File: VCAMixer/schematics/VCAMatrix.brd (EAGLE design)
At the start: 120 x 100 mm, 293 parts, among them IC1 QUAD_OPAMPD, IC2 TL074D, IC4 TL072D, Q1 BC846ALT1SMD, Q10 BSS123, Q2 BC846ALT1SMD, Q3 BC846ALT1SMD, Q4 BC846ALT1SMD, Q5 BC846ALT1SMD, Q6 BC846ALT1SMD, Q7 BC846ALT1SMD, Q8 BC846ALT1SMD, Q9 BSS84, X1 53048-05, X2 53048-05

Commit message: Board and Schematic Updated
Begin routing for input and output circuitry.
Schottky Diode used for power rail protection.
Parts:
- removed VCA1:D1, VCA2:D1, VCA3:D1, VCA4:D1: B130LAW-7-F, diode:SOD123
- added D3: BAT54A, diode:SOT23
- U$1, U$2: value RTRIM-3362P -> (none); device GeekAmmo:RTRIM3362P -> resistor:RTRIM64W
- moved R42 275.3 mm to (117.2, 17.8), turned to 90 degrees
- moved JP1 260.4 mm to (99.1, 76.2)
- moved R38 260.0 mm to (91.4, -16.5)
- moved VCA4:R3 246.1 mm to (117.2, 21.6), turned to 90 degrees
- moved VCA1:R3 243.4 mm to (114.3, 80.0), turned to 90 degrees
- moved JP3 242.9 mm to (72.4, 76.2)
- moved Q2 242.3 mm to (150.4, -30.9)
- moved VCA3:R3 239.2 mm to (117.6, 40.9), turned to 90 degrees
- moved VCA2:R3 238.8 mm to (117.2, 61.0), turned to 90 degrees
- moved VCA4:C14 238.4 mm to (117.2, 25.7), turned to 90 degrees
- moved VCA2:C14 238.3 mm to (118.1, 65.1), turned to 90 degrees
- moved C3 238.3 mm to (78.7, -16.5)
- moved C4 238.3 mm to (73.7, -16.5)
- moved C5 238.3 mm to (68.6, -16.5)
- moved C6 238.3 mm to (63.5, -16.5)
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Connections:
- net -12V: now also D3.3; no longer VCA1:D1.A, VCA2:D1.A, VCA3:D1.A, VCA4:D1.A
- net GND: now also D3.1, D3.2; no longer VCA1:D1.C, VCA2:D1.C, VCA3:D1.C, VCA4:D1.C
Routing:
- net -12V: track 0.00 -> 223.6 mm, vias 0 -> 7
- net +12V: track 0.00 -> 221.1 mm, vias 0 -> 13
- net CV_DD: track 0.00 -> 104.4 mm, vias 0 -> 1
- net GND: track 0.00 -> 78.7 mm, vias 0 -> 49
- net N$34: track 0.00 -> 76.2 mm, vias 0 -> 3
- net VCA4:IC2_4: track 0.00 -> 66.8 mm, vias 0 -> 2
- net VCA3:IC2_4: track 0.00 -> 66.5 mm, vias 0 -> 2
- net VCA2:IC2_5: track 0.00 -> 57.2 mm
- net CV_DB: track 0.00 -> 54.7 mm, vias 0 -> 1
- net CV_DC: track 0.00 -> 52.8 mm, vias 0 -> 1
- net CV_DA: track 0.00 -> 51.8 mm, vias 0 -> 1
- net N$18: track 0.00 -> 51.2 mm, vias 0 -> 4
- net N$82: track 0.00 -> 46.2 mm, vias 0 -> 3
- net VCA3:IC2_2: track 0.00 -> 41.8 mm
- net VCA1:IC2_2: track 0.00 -> 41.8 mm, vias 0 -> 2
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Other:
- board size 120 x 100 mm -> 119.8 x 101.3 mm

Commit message: Latest update on VCA Matrix Board
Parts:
- moved Q9 191.0 mm to (111.0, 22.5)
- moved R5 107.1 mm to (109.9, 96.8)
- moved R3 105.7 mm to (77.5, 80.0), turned to 270 degrees
- moved R13 102.5 mm to (81.3, 51.4), turned to 180 degrees
- moved R14 93.5 mm to (78.7, 37.8), turned to 270 degrees
- moved R6 92.5 mm to (102.6, 81.3), turned to 270 degrees
- moved R2 90.3 mm to (77.5, 57.8), turned to 270 degrees
- moved R10 85.9 mm to (107.7, 53.5), turned to 270 degrees
- moved Q2 82.7 mm to (75.8, 4.70), turned to 180 degrees
- moved R19 80.8 mm to (75.9, 38.4), turned to 180 degrees
- moved R15 67.4 mm to (109.6, 38.2), turned to 180 degrees
- moved R16 67.1 mm to (106.4, 38.4), turned to 180 degrees
- moved Q3 65.2 mm to (79.4, 4.76), turned to 180 degrees
- moved R1 64.5 mm to (80.0, 7.94), turned to 180 degrees
- moved R40 63.5 mm to (72.7, 49.2), turned to 180 degrees
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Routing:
- net N$34: track 76.2 -> 226.4 mm, vias 3 -> 17
- net -12V: track 223.6 -> 358.3 mm, vias 7 -> 13
- net N$47: track 0.00 -> 107.7 mm, vias 0 -> 6
- net N$11: track 0.00 -> 106.9 mm, vias 0 -> 11
- net CV_DD: track 104.4 -> 4.23 mm, vias 1 -> 0
- net N$82: track 46.2 -> 132.5 mm, vias 3 -> 4
- net N$58: track 2.32 -> 86.7 mm, vias 0 -> 6
- net CLAMP_REF: track 30.8 -> 110.3 mm, vias 0 -> 4
- net N$3: track 28.9 -> 104.1 mm, vias 3 -> 6
- net +12V: track 221.1 -> 290.9 mm, vias 13 -> 24
- net N$8: track 5.45 -> 67.6 mm, vias 0 -> 2
- net N$33: track 0.00 -> 60.4 mm, vias 0 -> 1
- net N$78: track 0.00 -> 52.6 mm, vias 0 -> 2
- net N$24: track 0.00 -> 52.2 mm, vias 0 -> 2
- net N$54: track 0.00 -> 43.2 mm, vias 0 -> 2
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
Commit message: Latest Update To VCA Board
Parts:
- moved R45 31.8 mm to (73.8, 1.65)
- moved R47 26.7 mm to (86.2, 11.2)
- moved Q7 18.9 mm to (99.9, 2.60)
- moved VCA1:R13 18.7 mm to (76.0, 79.1)
- moved VCA4:R43 16.1 mm to (84.3, 78.5)
- moved R35 14.4 mm to (67.8, 15.6)
- moved VCA4:R15 12.7 mm to (71.9, 20.1), turned to 90 degrees
- moved VCA2:C1 12.3 mm to (90.0, 73.4), turned to 180 degrees
- moved R17 12.2 mm to (97.0, 15.6)
- moved C2 12.2 mm to (98.6, 8.63)
- moved R41 12.2 mm to (100.5, 8.63)
- moved VCA1:R21 11.9 mm to (77.4, 81.8)
- moved VCA1:R9 11.9 mm to (74.2, 81.8)
- moved VCA3:R13 11.7 mm to (60.8, 74.3)
- moved VCA1:R15 11.6 mm to (72.0, 81.8)
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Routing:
- net GND: track 83.5 -> 225.9 mm, vias 52 -> 62
- net +12V: track 290.9 -> 317.8 mm, vias 24 -> 28
- net N$3: track 104.1 -> 130.2 mm, vias 6 -> 8
- net N$60: track 3.21 -> 21.7 mm, vias 0 -> 2
- net N$11: track 106.9 -> 90.4 mm, vias 11 -> 10
- net VCA4:N$7: track 7.20 -> 22.0 mm
- net CV_AA: track 3.99 -> 13.0 mm
- net VCA4:IC2_4: track 62.2 -> 71.1 mm
- net N$51: track 0.00 -> 7.67 mm
- net CV_DC: track 13.1 -> 6.67 mm
- net VCA1:IC2_5: track 19.7 -> 13.6 mm
- net N$24: track 52.2 -> 57.6 mm
- net OUTPUT_B: track 21.0 -> 26.3 mm, vias 1 -> 2
- net N$22: track 33.7 -> 28.4 mm
- net IN_A: track 0.00 -> 4.98 mm
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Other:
- board size 119.8 x 101.3 mm -> 116 x 100.3 mm

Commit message: Bottom Board Completed
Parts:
- moved R45 28.4 mm to (96.7, 18.5)
- moved R47 18.5 mm to (104.6, 9.59), turned to 270 degrees
- moved R33 17.9 mm to (97.1, 15.5), turned to 180 degrees
- moved R37 16.4 mm to (106.2, 13.1), turned to 270 degrees
- moved R7 11.6 mm to (83.5, 10.9)
- moved C5 8.91 mm to (87.5, 1.97)
- moved C2 8.90 mm to (103.7, 1.33), turned to 0 degrees
- moved R17 7.25 mm to (99.9, 8.95), turned to 270 degrees
- moved R24 6.38 mm to (76.4, 10.5)
- moved C3 6.30 mm to (67.8, 20.1), turned to 270 degrees
- moved R41 5.93 mm to (94.8, 10.2), turned to 180 degrees
- moved R23 5.84 mm to (91.6, 10.2), turned to 180 degrees
- moved C4 5.13 mm to (87.5, 3.24)
- moved C1 4.77 mm to (65.3, 1.97), turned to 180 degrees
- moved R12 2.54 mm to (70.3, 9.59)
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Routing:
- net GND: track 225.9 -> 321.7 mm, vias 62 -> 76
- net +12V: track 317.8 -> 387.0 mm, vias 28 -> 32
- net OUTPUT_B: track 26.3 -> 80.7 mm, vias 2 -> 4
- net N$66: track 0.38 -> 49.2 mm, vias 0 -> 4
- net N$59: track 30.1 -> 74.3 mm, vias 1 -> 3
- net -12V: track 355.3 -> 399.1 mm, vias 13 -> 19
- net OUTPUT_A: track 0.00 -> 41.2 mm, vias 0 -> 2
- net N$58: track 87.6 -> 127.1 mm, vias 6 -> 8
- net N$11: track 90.4 -> 118.1 mm, vias 10 -> 11
- net N$22: track 28.4 -> 54.8 mm, vias 3 -> 6
- net OUTPUT_C: track 0.00 -> 25.6 mm, vias 0 -> 2
- net N$47: track 108.2 -> 131.6 mm, vias 6 -> 7
- net N$45: track 0.00 -> 20.5 mm, vias 0 -> 2
- net IN_A: track 4.98 -> 24.6 mm, vias 0 -> 2
- net N$82: track 133.3 -> 152.1 mm
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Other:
- board size 116 x 100.3 mm -> 114.8 x 100 mm

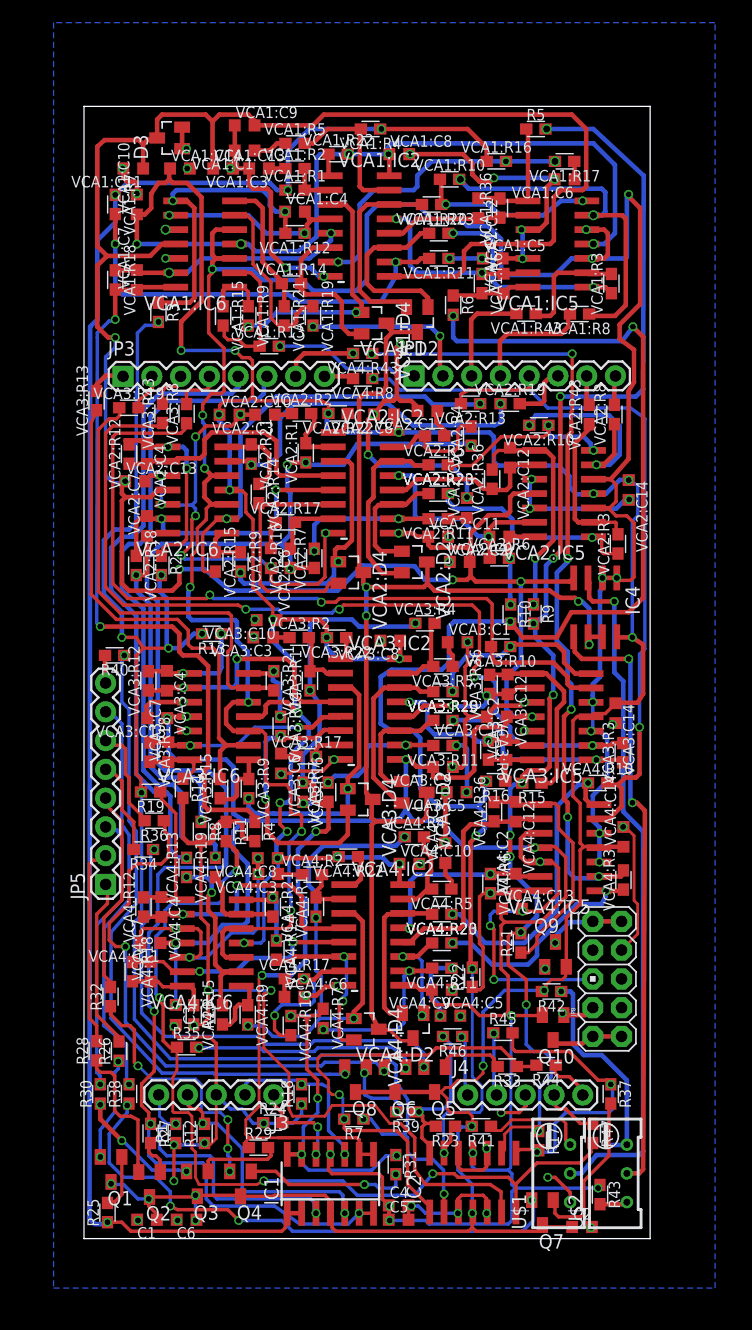
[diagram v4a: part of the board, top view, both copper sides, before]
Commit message: added top ground plane and ajusted routing
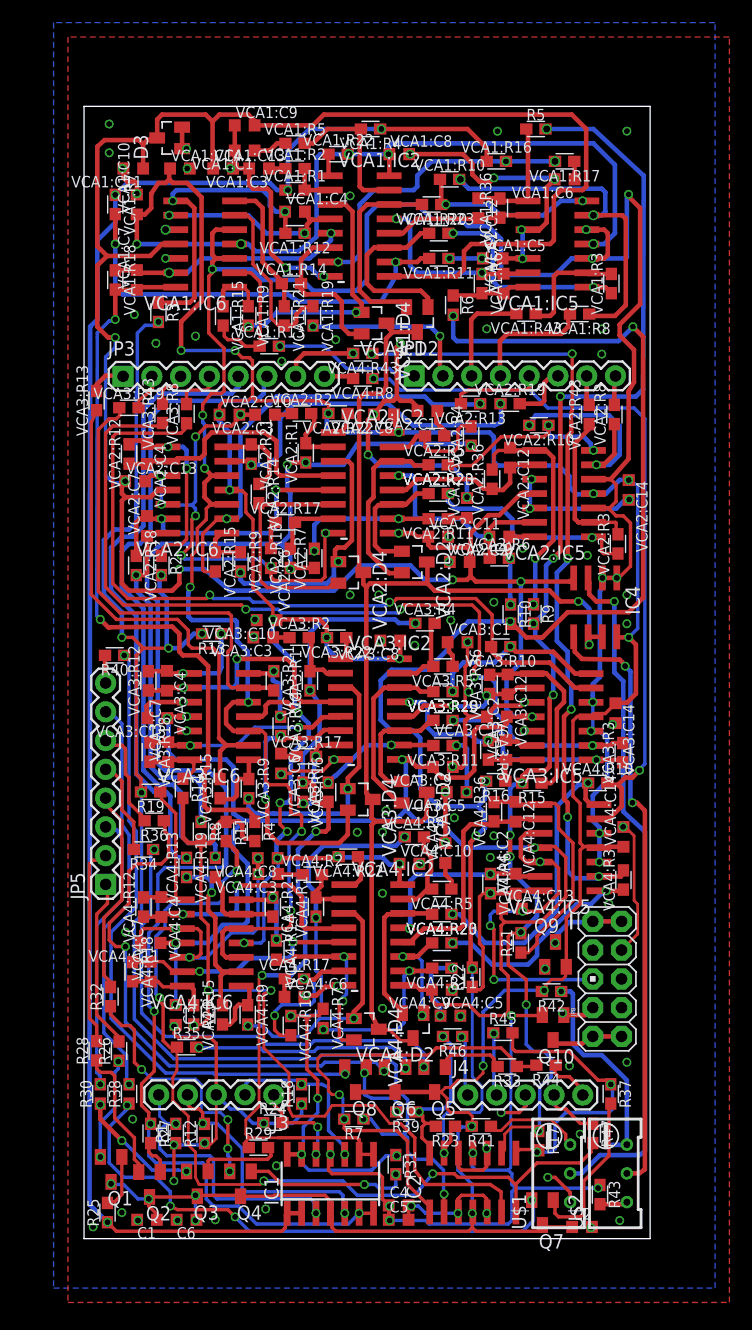
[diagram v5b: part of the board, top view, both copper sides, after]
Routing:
- net N$47: track 131.6 -> 129.5 mm
- net VCA3:IC2_2: track 71.9 -> 70.9 mm
- net -12V: track 399.1 -> 398.0 mm
- net N$34: track 230.4 -> 229.3 mm
- net VCA3:N$23: track 12.2 -> 11.4 mm
- net VCA3:IC2_1: track 16.6 -> 15.8 mm
- net OUTPUT_B: track 80.7 -> 80.1 mm
- net N$49: track 12.6 -> 12.0 mm
- net N$23: track 77.4 -> 76.8 mm
- net VCA2:N$7: track 21.8 -> 21.3 mm
- net GND: track 321.7 -> 321.2 mm, vias 76 -> 119
- net N$13: track 9.77 -> 9.22 mm
- net CLAMP_REF: track 106.5 -> 106.6 mm, vias 4 -> 2
- added copper zone on layer 1, net GND

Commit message: Routing completed for Top Board
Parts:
- moved X2 4.45 mm to (5.78, 38.9), turned to 90 degrees
- turned X1 to 270 degrees
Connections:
- removed net N$80: OUTD.P$3
- removed net N$81: OUTC.P$3
- removed net N$83: OUTB.P$3
- removed net N$84: OUTA.P$3
- net OUT_A: now also OUTA.P$3
- net OUT_B: now also OUTB.P$3
- net OUT_C: now also OUTC.P$3
- net OUT_D: now also OUTD.P$3
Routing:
- net LED_8: track 2.45 -> 66.5 mm
- net OUT_A: track 4.24 -> 67.3 mm
- net LED_3: track 24.7 -> 79.1 mm
- net N$75: track 0.00 -> 54.2 mm
- net N$76: track 0.00 -> 50.3 mm, vias 0 -> 1
- net LED_4: track 18.4 -> 68.7 mm, vias 0 -> 1
- net N$74: track 0.00 -> 48.5 mm
- net CV_DD: track 2.61 -> 47.0 mm
- net N$70: track 0.00 -> 44.2 mm, vias 0 -> 1
- net CV_AA: track 13.0 -> 57.2 mm
- net CV_BA: track 8.10 -> 51.2 mm
- net CV_CD: track 4.25 -> 46.6 mm
- net LED_7: track 35.8 -> 76.4 mm
- net N$73: track 0.00 -> 39.9 mm, vias 0 -> 1
- net OUT_B: track 5.09 -> 44.7 mm
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
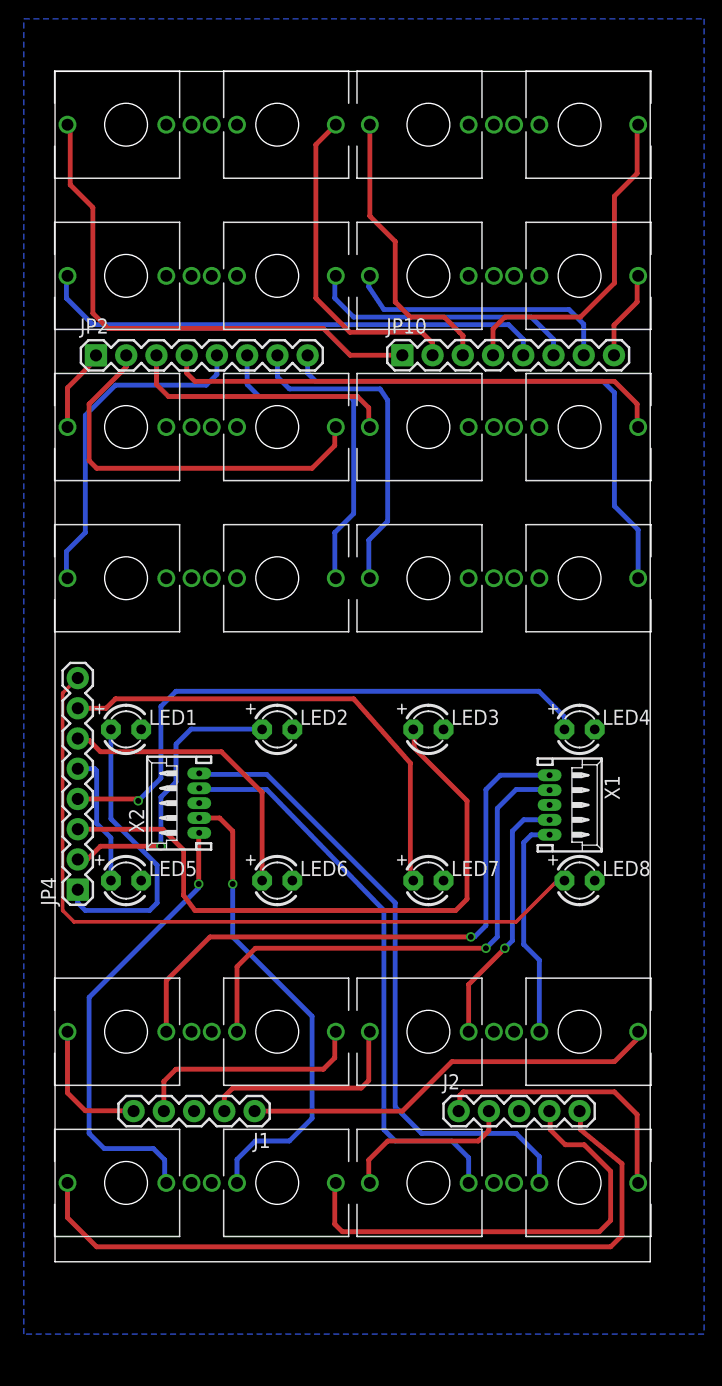
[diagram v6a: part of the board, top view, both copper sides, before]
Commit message: added in/out headers and routing
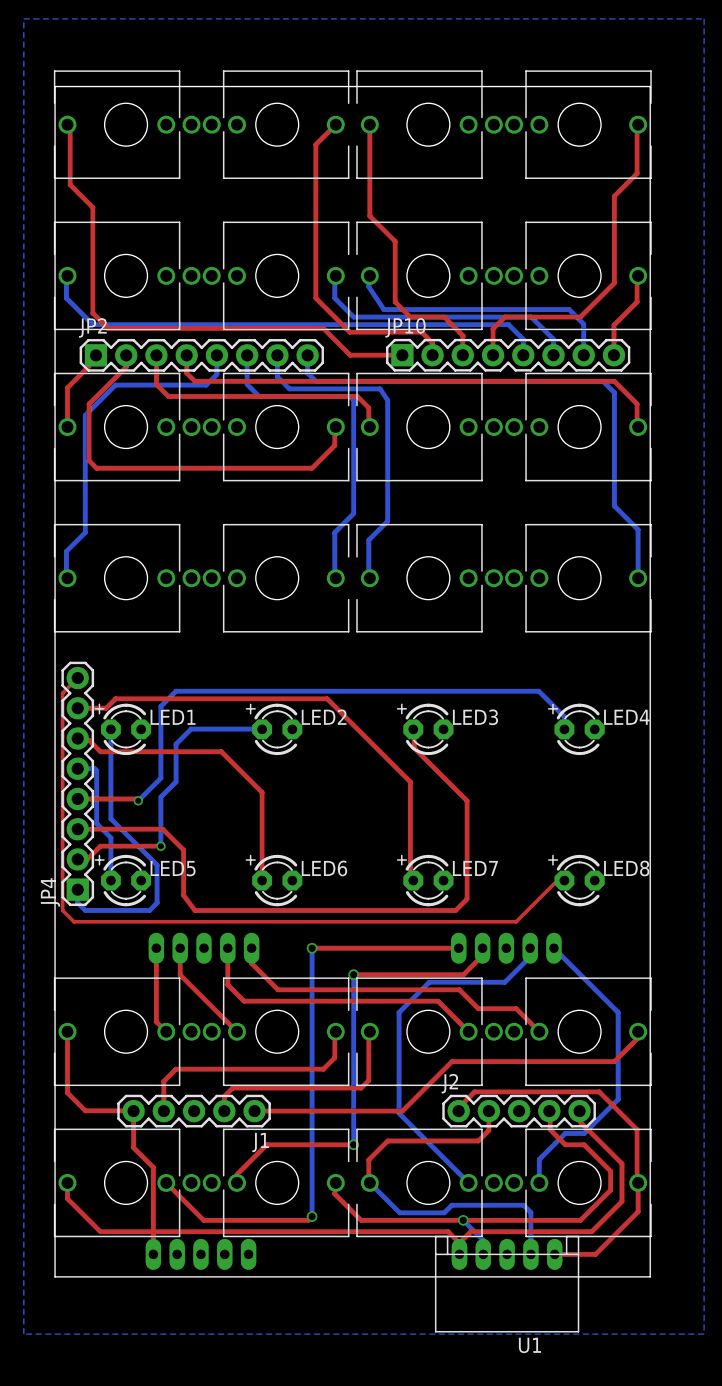
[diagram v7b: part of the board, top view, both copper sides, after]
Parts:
- removed X1, X2: 53048-05, con-molex:53048-05
- added U1, U2, U3, U4: CON-JST_PH_5W, Rebel:CON-JST_PH_5W
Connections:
- net GND: now also U1.P3, U2.P3, U3.P3, U4.P3; no longer X1.3, X2.3
- net IN_A: now also U2.P1
- net IN_B: now also U2.P2
- net IN_C: now also U2.P4
- net IN_D: now also U2.P5
- net N$55: now also U3.P5; no longer X2.5
- net N$70: now also U4.P4; no longer X1.4
- net N$71: now also U4.P2; no longer X1.2
- net N$72: now also U4.P1; no longer X1.1
- net N$73: now also U3.P4; no longer X2.4
- net N$74: now also U3.P2; no longer X2.2
- net N$75: now also U3.P1; no longer X2.1
- net N$76: now also U4.P5; no longer X1.5
- net OUT_A: now also U1.P1
- net OUT_B: now also U1.P2
- net OUT_C: now also U1.P4
- net OUT_D: now also U1.P5
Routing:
- net N$76: track 50.3 -> 7.36 mm, vias 1 -> 0
- net N$70: track 44.2 -> 8.99 mm, vias 1 -> 0
- net N$75: track 54.2 -> 25.6 mm
- net OUT_C: track 20.8 -> 39.4 mm
- net N$74: track 48.5 -> 30.4 mm
- net IN_A: track 36.0 -> 48.7 mm
- net N$55: track 38.3 -> 48.5 mm, vias 1 -> 2
- net OUT_D: track 29.0 -> 38.7 mm
- net N$72: track 18.9 -> 27.8 mm
- net N$71: track 21.9 -> 24.9 mm, vias 1 -> 0
- net OUT_A: track 67.3 -> 65.2 mm
- net N$73: track 39.9 -> 38.0 mm, vias 1 -> 2
- net LED_7: track 76.4 -> 75.3 mm
- net OUT_B: track 44.7 -> 44.5 mm, vias 0 -> 1
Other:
- board size 114.8 x 100 mm -> 114.8 x 101.2 mm
